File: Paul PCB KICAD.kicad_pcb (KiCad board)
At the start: 2 copper layers, 81 parts, among them U1 ATmega32U4-AU

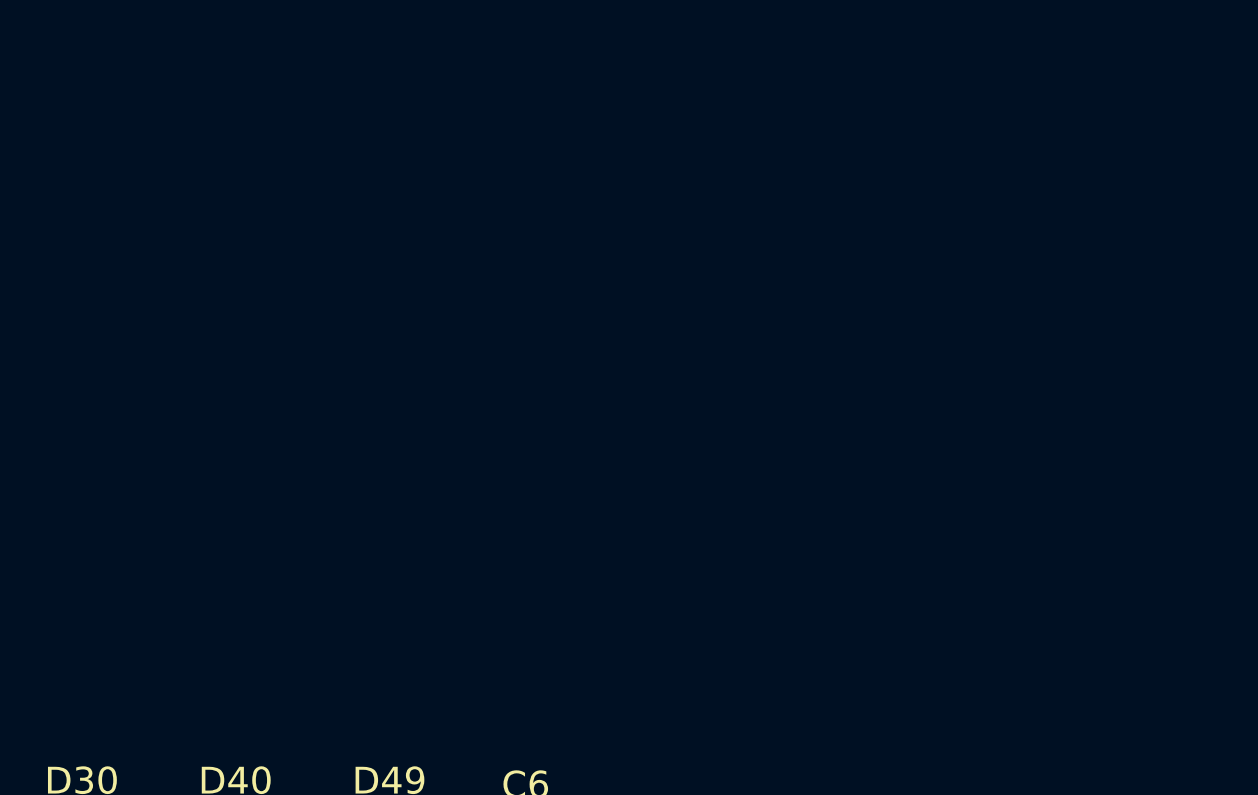
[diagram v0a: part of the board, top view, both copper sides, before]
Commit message: Updated USB to 4084 GCT
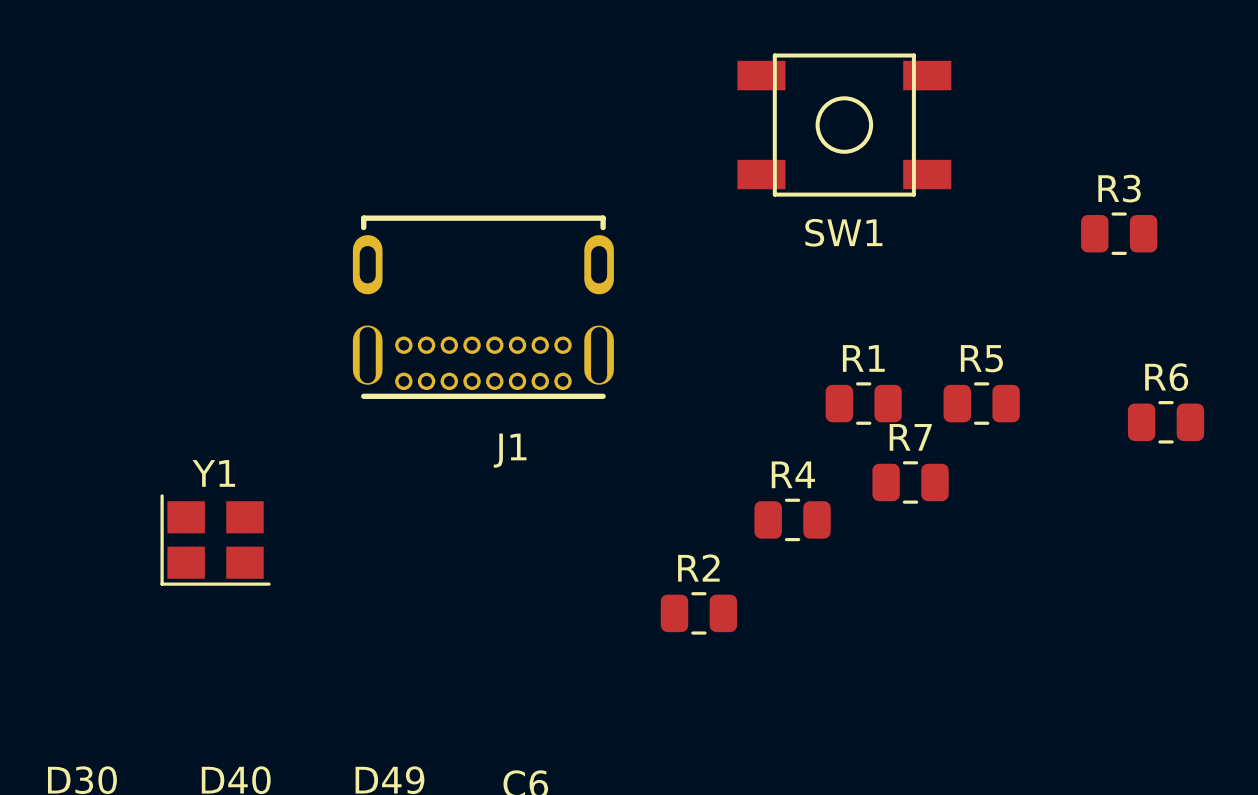
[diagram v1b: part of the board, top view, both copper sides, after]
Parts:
- added J1: USB4085-GF-A_REVA, 4085 USB Connector GCT:GCT_USB4085-GF-A_REVA, F.Cu at (105.6, 70.6)
- added R1: 1M, Resistor_SMD:R_0805_2012Metric, F.Cu at (119.8, 75.5)
- added R2: 5.1k, Resistor_SMD:R_0805_2012Metric, F.Cu at (113.6, 83.3)
- added R3: 5.1k, Resistor_SMD:R_0805_2012Metric, F.Cu at (129.3, 69.2)
- added R4: 22, Resistor_SMD:R_0805_2012Metric, F.Cu at (117.1, 79.8)
- added R5: 22, Resistor_SMD:R_0805_2012Metric, F.Cu at (124.2, 75.5)
- added R6: 10k, Resistor_SMD:R_0805_2012Metric, F.Cu at (131.1, 76.2)
- added R7: 10k, Resistor_SMD:R_0805_2012Metric, F.Cu at (121.5, 78.5)
- added SW1: SW_Push, random-keyboard-parts:SKQG-1155865, F.Cu at (119.1, 65.1)
- added Y1: 16MHz, Crystal:Crystal_SMD_3225-4Pin_3.2x2.5mm, F.Cu at (95.6, 80.6)
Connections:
- C1 pad 1: Net-(C1-Pad1) -> GND
- C1 pad 2: GND -> Net-(C1-Pad2)

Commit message: Added Near Final Edge Cut and Positioned Switch footprints
Need to add the diodes and caps and some cleanup
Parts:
- removed J1: USB4085-GF-A_REVA, 4085 USB Connector GCT:GCT_USB4085-GF-A_REVA
- added MX1: MX-NoLED, MX_Only:MXOnly-1U-Hotswap, F.Cu at (26.7, -83.2)
- added MX10: MX-NoLED, MX_Only:MXOnly-1U-Hotswap, F.Cu at (209.6, -82.6)
- added MX100: MX-NoLED, MX_Only:MXOnly-1.5U-Hotswap, F.Cu at (9.96, -64.1)
- added MX101: MX-NoLED, MX_Only:MXOnly-1U-Hotswap, F.Cu at (33.8, -64.1)
- added MX102: MX-NoLED, MX_Only:MXOnly-1U-Hotswap, F.Cu at (54.0, -64.0)
- added MX103: MX-NoLED, MX_Only:MXOnly-1U-Hotswap, F.Cu at (72.9, -61.3)
- added MX104: MX-NoLED, MX_Only:MXOnly-1U-Hotswap, F.Cu at (91.7, -58.7)
- added MX105: MX-NoLED, MX_Only:MXOnly-1U-Hotswap, F.Cu at (110.6, -56.0)
- added MX106: MX-NoLED, MX_Only:MXOnly-1U-Hotswap, F.Cu at (146.2, -54.4)
- added MX107: MX-NoLED, MX_Only:MXOnly-1U-Hotswap, F.Cu at (165.1, -57.1)
- added MX108: MX-NoLED, MX_Only:MXOnly-1U-Hotswap, F.Cu at (183.9, -59.7)
- added MX109: MX-NoLED, MX_Only:MXOnly-1U-Hotswap, F.Cu at (202.8, -62.4)
- added MX11: MX-NoLED, MX_Only:MXOnly-1U-Hotswap, F.Cu at (229.8, -83.2)
- added MX110: MX-NoLED, MX_Only:MXOnly-1U-Hotswap, F.Cu at (223.1, -64.1)
- added MX111: MX-NoLED, MX_Only:MXOnly-1U-Hotswap, F.Cu at (242.2, -64.1)
- added MX112: MX-NoLED, MX_Only:MXOnly-1U-Hotswap, F.Cu at (261.2, -64.1)
- added MX113: MX-NoLED, MX_Only:MXOnly-1.5U-Hotswap, F.Cu at (285.0, -64.1)
- added MX114: MX-NoLED, Rotary_Encoder:RotaryEncoder_Alps_EC11E-Switch_Vertical_H20mm, F.Cu at (308.6, -85.7)
- added MX12: MX-NoLED, MX_Only:MXOnly-1U-Hotswap, F.Cu at (248.8, -83.2)
- added MX13: MX-NoLED, MX_Only:MXOnly-1U-Hotswap, F.Cu at (267.9, -83.2)
- added MX14: MX-NoLED, MX_Only:MXOnly-1U-Hotswap, F.Cu at (286.9, -83.2)
- added MX2: MX-NoLED, MX_Only:MXOnly-1U-Hotswap, F.Cu at (47.2, -84.2)
- added MX200: MX-NoLED, MX_Only:MXOnly-1.75U-Hotswap, F.Cu at (9.66, -45.1)
- added MX201: MX-NoLED, MX_Only:MXOnly-1U-Hotswap, F.Cu at (35.9, -45.1)
- added MX202: MX-NoLED, MX_Only:MXOnly-1U-Hotswap, F.Cu at (56.1, -44.4)
- added MX203: MX-NoLED, MX_Only:MXOnly-1U-Hotswap, F.Cu at (74.9, -41.8)
- added MX204: MX-NoLED, MX_Only:MXOnly-1U-Hotswap, F.Cu at (93.8, -39.1)
- added MX205: MX-NoLED, MX_Only:MXOnly-1U-Hotswap, F.Cu at (112.7, -36.5)
- added MX206: MX-NoLED, MX_Only:MXOnly-1U-Hotswap, F.Cu at (153.6, -36.2)
- added MX207: MX-NoLED, MX_Only:MXOnly-1U-Hotswap, F.Cu at (172.5, -38.9)
- added MX208: MX-NoLED, MX_Only:MXOnly-1U-Hotswap, F.Cu at (191.3, -41.5)
- added MX209: MX-NoLED, MX_Only:MXOnly-1U-Hotswap, F.Cu at (210.2, -44.2)
- added MX210: MX-NoLED, MX_Only:MXOnly-1U-Hotswap, F.Cu at (230.3, -45.1)
- added MX211: MX-NoLED, MX_Only:MXOnly-1U-Hotswap, F.Cu at (249.3, -45.1)
- added MX212: MX-NoLED, MX_Only:MXOnly-2.25U-Hotswap, F.Cu at (280.3, -45.1)
- added MX214: MX-NoLED, MX_Only:MXOnly-1U-Hotswap, F.Cu at (316.1, -59.8)
- added MX3: MX-NoLED, MX_Only:MXOnly-1U-Hotswap, F.Cu at (66.1, -81.5)
- added MX300: MX-NoLED, MX_Only:MXOnly-2.25U-Hotswap, F.Cu at (11.7, -26.0)
- added MX301: MX-NoLED, MX_Only:MXOnly-1U-Hotswap, F.Cu at (42.7, -26.0)
- added MX302: MX-NoLED, MX_Only:MXOnly-1U-Hotswap, F.Cu at (62.8, -24.3)
- added MX303: MX-NoLED, MX_Only:MXOnly-1U-Hotswap, F.Cu at (81.7, -21.6)
- added MX304: MX-NoLED, MX_Only:MXOnly-1U-Hotswap, F.Cu at (100.6, -19.0)
- added MX305: MX-NoLED, MX_Only:MXOnly-1U-Hotswap, F.Cu at (119.4, -16.3)
- added MX306: MX-NoLED, MX_Only:MXOnly-1U-Hotswap, F.Cu at (165.7, -18.7)
- added MX307: MX-NoLED, MX_Only:MXOnly-1U-Hotswap, F.Cu at (184.5, -21.4)
- added MX308: MX-NoLED, MX_Only:MXOnly-1U-Hotswap, F.Cu at (203.4, -24.0)
- added MX309: MX-NoLED, MX_Only:MXOnly-1U-Hotswap, F.Cu at (223.1, -26.0)
- added MX310: MX-NoLED, MX_Only:MXOnly-1U-Hotswap, F.Cu at (242.2, -26.0)
- added MX311: MX-NoLED, MX_Only:MXOnly-1U-Hotswap, F.Cu at (261.2, -26.0)
- added MX312: MX-NoLED, MX_Only:MXOnly-1U-Hotswap, F.Cu at (285.2, -21.1)
- added MX314: MX-NoLED, MX_Only:MXOnly-1U-Hotswap, F.Cu at (316.1, -40.7)
- added MX4: MX-NoLED, MX_Only:MXOnly-1U-Hotswap, F.Cu at (85.0, -78.9)
- added MX400: MX-NoLED, MX_Only:MXOnly-1.25U-Hotswap, F.Cu at (6.98, -6.98)
- added MX401: MX-NoLED, MX_Only:MXOnly-1.25U-Hotswap, F.Cu at (30.8, -7.00)
- added MX402: MX-NoLED, MX_Only:MXOnly-1.25U-Hotswap, F.Cu at (62.6, -5.06)
- added MX404: MX-NoLED, MX_Only:MXOnly-2.75U-Hotswap-ReversedStabilizers, F.Cu at (100.3, 0.24)
- added MX405: MX-NoLED, MX_Only:MXOnly-1U-Hotswap, F.Cu at (146.8, -16.1)
- added MX406: MX-NoLED, MX_Only:MXOnly-2.25U-Hotswap-ReversedStabilizers, F.Cu at (170.7, -0.17)
- added MX408: MX-NoLED, MX_Only:MXOnly-1U-Hotswap, F.Cu at (201.3, -4.48)
- added MX409: MX-NoLED, MX_Only:MXOnly-1U-Hotswap, F.Cu at (223.1, -7.01)
- added MX410: MX-NoLED, MX_Only:MXOnly-1U-Hotswap, F.Cu at (242.2, -7.01)
- added MX411: MX-NoLED, MX_Only:MXOnly-1U-Hotswap, F.Cu at (266.2, -2.06)
- added MX412: MX-NoLED, MX_Only:MXOnly-1U-Hotswap, F.Cu at (285.2, -2.05)
- added MX414: MX-NoLED, MX_Only:MXOnly-1U-Hotswap, F.Cu at (304.2, -2.06)
- added MX5: MX-NoLED, MX_Only:MXOnly-1U-Hotswap, F.Cu at (103.8, -76.2)
- added MX6: MX-NoLED, MX_Only:MXOnly-1U-Hotswap, F.Cu at (122.7, -73.6)
- added MX7: MX-NoLED, MX_Only:MXOnly-1U-Hotswap, F.Cu at (153.0, -74.6)
- added MX8: MX-NoLED, MX_Only:MXOnly-1U-Hotswap, F.Cu at (171.9, -77.3)
- added MX9: MX-NoLED, MX_Only:MXOnly-1U-Hotswap, F.Cu at (190.7, -79.9)
- added USB1: HRO-TYPE-C-31-M-12, Type-C:HRO-TYPE-C-31-M-12, F.Cu at (159.5, -101.3)
- moved MX0 186.8 mm to (7.67, -83.2)
- moved D4 164.9 mm to (81.1, -73.2)
- moved U1 149.5 mm to (129.7, -48.5), turned to 270 degrees
- moved R3 41.8 mm to (87.7, 72.8)
- moved R1 36.6 mm to (83.3, 72.8)
- moved C1 34.2 mm to (83.3, 69.8)
- moved R2 29.2 mm to (87.8, 69.8)
- renumbered D1 to D0, D6 to D1, D49 to D10, D2 to D100, D7 to D101, D12 to D102, D17 to D103, D21 to D104, D26 to D105, D31 to D106, D36 to D107, D40 to D108, D45 to D109, D54 to D11, D50 to D110, D55 to D111, D60 to D112, D65 to D113, D67 to D114, D59 to D12, D64 to D13, D66 to D14, D11 to D2, D3 to D200, D8 to D201, D13 to D202, D18 to D203, D22 to D204, D27 to D205, D32 to D206, D37 to D207, D41 to D208, D46 to D209, D51 to D210, D56 to D211, D61 to D212, D68 to D214, D16 to D3, D4 to D300, D9 to D301, D14 to D302, D19 to D303, D23 to D304, D28 to D305, D33 to D306, D38 to D307, D42 to D308, D47 to D309, D52 to D310, D57 to D311, D62 to D312, D69 to D314, D20 to D4, D5 to D400, D10 to D401, D15 to D402, D24 to D404, D29 to D405, D34 to D406, D43 to D408, D48 to D409, D53 to D410, D58 to D411, D63 to D412, D70 to D414, D25 to D5, D30 to D6, D35 to D7, D39 to D8, D44 to D9, MX1 to MX0
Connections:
- U1 pad 15: GND -> Net-(U1-Pad15)
- U1 pad 23: GND -> Net-(U1-Pad15)
- U1 pad 35: GND -> Net-(U1-Pad15)
- U1 pad 43: GND -> Net-(U1-Pad15)
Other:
- board outline added: 330.9 x 112.7 mm

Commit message: More PCB Completed
Added Mounting Holes as pads
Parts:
- removed MX114: MX-NoLED, Rotary_Encoder:RotaryEncoder_Alps_EC11E-Switch_Vertical_H20mm
- added 2.5: 2.5_Mount, MountingHole:MountingHole_2.5mm_Pad, F.Cu at (133.1, -35.4)
- added 2.5: 2.5_Mount, MountingHole:MountingHole_2.5mm_Pad, F.Cu at (17.2, -80.2)
- added 2.5: 2.5_Mount, MountingHole:MountingHole_2.5mm_Pad, F.Cu at (232.6, -16.5)
- added 2.5: 2.5_Mount, MountingHole:MountingHole_2.5mm_Pad, F.Cu at (301.5, -83.2)
- added 2.5: 2.5_Mount, MountingHole:MountingHole_2.5mm_Pad, F.Cu at (1.15, -54.6)
- added 2.5: 2.5_Mount, MountingHole:MountingHole_2.5mm_Pad, F.Cu at (77.3, -3.00)
- added 2.5: 2.5_Mount, MountingHole:MountingHole_2.5mm_Pad, F.Cu at (219.9, -80.4)
- added 2.5: 2.5_Mount, MountingHole:MountingHole_2.5mm_Pad, F.Cu at (18.9, -7.00)
- added 2.5: 2.5_Mount, MountingHole:MountingHole_2.5mm_Pad, F.Cu at (162.9, -73.0)
- added 2.5: 2.5_Mount, MountingHole:MountingHole_2.5mm_Pad, F.Cu at (294.8, -11.6)
- added 2.5: 2.5_Mount, MountingHole:MountingHole_2.5mm_Pad, F.Cu at (94.0, -74.6)
- added 2.5: 2.5_Mount, MountingHole:MountingHole_2.5mm_Pad, F.Cu at (149.4, 2.33)
- added 2.5: 2.5_Mount, MountingHole:MountingHole_2.5mm_Pad, F.Cu at (302.3, -47.4)
- added RotaryEncoder1: Rotary_Encoder_Switch, Rotary_Encoder:RotaryEncoder_Alps_EC11E-Switch_Vertical_H20mm, F.Cu at (323.6, -80.7)
- C1, C2, C3, C4, C5, C6, C7, C8, D0, D1, D10, D100, D101, D102, D103, D104, D105, D106, D107, D108, D109, D11, D110, D111, D112, D113, D114, D12, D13, D14, D2, D200, D201, D202, D203, D204, D205, D206, D207, D208, D209, D210, D211, D212, D214, D3, D300, D301, D302, D303, D304, D305, D306, D307, D308, D309, D310, D311, D312, D314, D4, D400, D401, D402, D404, D405, D406, D408, D409, D410, D411, D412, D414, D5, D6, D7, D8, D9, R1, R6, R7, U1, Y1: moved to B.Cu
- moved D114 291.8 mm to (307.2, -73.8)
- moved D214 275.0 mm to (316.7, -54.8)
- moved D13 272.1 mm to (266.7, -78.6)
- moved D314 260.2 mm to (316.7, -33.3)
- moved D12 259.9 mm to (252.4, -78.6), turned to 270 degrees
- moved D14 256.7 mm to (288.1, -78.6)
- moved D111 251.8 mm to (242.9, -57.1)
- moved D113 248.7 mm to (285.8, -59.5)
- moved D11 247.9 mm to (231.0, -76.2)
- moved D414 242.7 mm to (307.2, 2.38)
- moved D212 239.7 mm to (281.0, -40.5)
- moved D312 229.0 mm to (288.1, -16.7)
- moved D412 226.3 mm to (290.5, 2.38), turned to 270 degrees
- moved D310 224.3 mm to (242.9, -21.4)
- moved D410 222.5 mm to (242.9, -2.38)
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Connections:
- net Net-(R4-Pad1) renamed /USB_N
- net Net-(R5-Pad1) renamed /USB_P
- D114 pad 2: Net-(D114-Pad2) -> Rot.Enc.2
- U1 pad 15: Net-(U1-Pad15) -> GND
- U1 pad 23: Net-(U1-Pad15) -> GND
- U1 pad 35: Net-(U1-Pad15) -> GND
- U1 pad 43: Net-(U1-Pad15) -> GND
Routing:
- net +5V: track 0.00 -> 123.3 mm, vias 0 -> 4
- net COL5: track 0.00 -> 97.8 mm, vias 0 -> 5
- net COL1: track 0.00 -> 87.8 mm, vias 0 -> 5
- net COL4: track 0.00 -> 85.6 mm, vias 0 -> 5
- net COL2: track 0.00 -> 85.6 mm, vias 0 -> 5
- net COL0: track 0.00 -> 82.1 mm, vias 0 -> 5
- net COL3: track 0.00 -> 66.3 mm, vias 0 -> 4
- net /USB_N: track 0.00 -> 54.5 mm, vias 0 -> 1
- net GND: track 0.00 -> 53.3 mm, vias 0 -> 5
- net /USB_P: track 0.00 -> 52.5 mm, vias 0 -> 3
- net Net-(C1-Pad2): track 0.00 -> 28.5 mm
- net VCC: track 0.00 -> 19.2 mm, vias 0 -> 2
- net Net-(C3-Pad1): track 0.00 -> 15.6 mm
- net Net-(C4-Pad1): track 0.00 -> 12.8 mm
- net D+: track 0.00 -> 9.04 mm
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- added copper zone on F.Cu, net GND
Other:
- outline, holes or cut-outs redrawn
- net class Power added: clearance 0.2, trace_width 0.4, via_dia 0.8, via_drill 0.4
- board text added: "MX114"

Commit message: Further Completion
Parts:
- R2, R3, SW1: moved to B.Cu
- moved SW1 42.5 mm to (140.1, -68.2), turned to 90 degrees
- moved R6 36.9 mm to (136.1, -65.6), turned to 90 degrees
- moved R4 23.8 mm to (138.8, -78.6), turned to 23.5 degrees
- moved R5 21.9 mm to (139.6, -76.7), turned to 23.5 degrees
- moved R1 14.9 mm to (166.1, -85.8), turned to 156.5 degrees
- moved D107 14.6 mm to (173.2, -63.0), turned to 278 degrees
- moved C1 14.4 mm to (166.9, -87.6), turned to 156.5 degrees
- moved D111 14.3 mm to (251.1, -68.8), turned to 270 degrees
- moved D102 13.5 mm to (63.3, -67.5), turned to 262 degrees
- moved D101 13.1 mm to (42.6, -68.8), turned to 270 degrees
- moved D103 13.1 mm to (82.2, -64.8), turned to 262 degrees
- moved D109 12.8 mm to (210.9, -68.3), turned to 278 degrees
- moved D104 12.7 mm to (101.0, -62.1), turned to 262 degrees
- moved D108 12.6 mm to (192.0, -65.7), turned to 278 degrees
- moved D112 12.6 mm to (270.4, -68.8), turned to 270 degrees
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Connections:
- net /USB_N renamed /Data_N
- net /USB_P renamed /Data_P
- net Net-(R6-Pad2) renamed /Reset
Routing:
- net ROW0: track 0.00 -> 288.1 mm
- net COL14: track 0.00 -> 128.9 mm
- net ROW1: track 0.00 -> 113.7 mm
- net COL6: track 0.00 -> 108.9 mm, vias 5 -> 7
- net COL12: track 0.00 -> 100.0 mm
- net GND: track 53.3 -> 153.1 mm, vias 5 -> 7
- net COL11: track 0.00 -> 96.2 mm
- net COL10: track 0.00 -> 89.6 mm
- net COL8: track 0.00 -> 86.7 mm
- net COL9: track 0.00 -> 85.5 mm
- net COL7: track 0.00 -> 66.3 mm
- net /Reset: track 0.00 -> 29.0 mm, vias 0 -> 2
- net COL13: track 0.00 -> 28.8 mm
- net /Data_N: track 54.5 -> 29.5 mm
- net /Data_P: track 52.5 -> 29.5 mm, vias 3 -> 1
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- added copper zone on B.Cu, net GND
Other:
- board size 330.9 x 112.7 mm -> 330.9 x 105.7 mm
- board text added: "Designed by Alfie Lockrey June 2021"
- board text added: "PaulPCB - V1.0"

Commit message: Finished Prelim Diode Placement
Beginning to Route Tracks
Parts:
- removed MX3: MX-NoLED, MX_Only:MXOnly-1U-Hotswap
- moved D214 24.0 mm to (292.7, -55.5)
- moved D314 18.3 mm to (298.4, -32.6)
- moved D206 15.1 mm to (161.4, -42.1), turned to 278 degrees
- moved D400 14.8 mm to (15.6, -12.8), turned to 90 degrees
- moved D307 14.6 mm to (192.5, -27.2), turned to 278 degrees
- moved D306 14.4 mm to (173.6, -24.6), turned to 278 degrees
- moved D304 14.4 mm to (109.9, -22.4), turned to 262 degrees
- moved D408 14.4 mm to (209.2, -10.3), turned to 278 degrees
- moved D311 14.3 mm to (270.1, -30.8), turned to 270 degrees
- moved D405 14.3 mm to (154.7, -21.9), turned to 98 degrees
- moved D210 14.2 mm to (238.9, -49.8), turned to 270 degrees
- moved D305 14.1 mm to (128.7, -19.8), turned to 262 degrees
- moved D411 14.1 mm to (274.9, -6.74), turned to 270 degrees
- moved D203 14.1 mm to (84.2, -45.3), turned to 262 degrees
- moved D204 13.8 mm to (103.1, -42.5), turned to 262 degrees
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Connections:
- D408 pad 1: Net-(D408-Pad1) -> ROW4
- MX408 pad 2: Net-(MX408-Pad2) -> Net-(D408-Pad2)
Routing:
- net ROW1: track 113.7 -> 281.4 mm
- net ROW2: track 0.00 -> 114.1 mm
- net Net-(D201-Pad2): track 0.00 -> 4.08 mm
- net Net-(D200-Pad2): track 0.00 -> 4.02 mm

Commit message: Finished V1.0
I think it may be done
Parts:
- added MX3: MX-NoLED, MX_Only:MXOnly-1U-Hotswap, F.Cu at (66.1, -81.5)
- F1, R4, R5: moved to B.Cu
- moved C6 4.09 mm to (137.6, -41.8), turned to 90 degrees
- moved C3 3.12 mm to (149.2, -46.8)
- moved C4 3.12 mm to (149.2, -49.6)
- moved Y1 3.12 mm to (144.6, -48.2)
- moved C8 1.22 mm to (125.4, -59.4)
- moved D414 1.16 mm to (295.4, 1.01)
- moved SW1 1.09 mm to (140.1, -69.2)
- moved R3 0.74 mm to (162.4, -82.4), turned to 180 degrees
- moved D409 0.74 mm to (226.4, -15.9)
- moved D400 0.74 mm to (15.5, -12.1), turned to 270 degrees
- moved C1 0.41 mm to (167.3, -87.5)
- moved R1 0.41 mm to (166.5, -85.7)
- moved C5 0.34 mm to (139.4, -51.2)
- moved R2 0.33 mm to (162.4, -84.4), turned to 180 degrees
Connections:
- RotaryEncoder1 pad C: Rot.Enc.C -> GND
- U1 pad 10: Net-(U1-Pad10) -> COL6
- U1 pad 11: Net-(U1-Pad11) -> COL7
- U1 pad 12: Net-(U1-Pad12) -> COL13
- U1 pad 18: Net-(U1-Pad18) -> COL8
- U1 pad 19: Net-(U1-Pad19) -> COL9
- U1 pad 20: Net-(U1-Pad20) -> COL10
- U1 pad 21: Net-(U1-Pad21) -> COL11
- U1 pad 22: Net-(U1-Pad22) -> ROW2
- U1 pad 25: Net-(U1-Pad25) -> Rot.Enc.A
- U1 pad 26: Net-(U1-Pad26) -> Rot.Enc.B
- U1 pad 27: Net-(U1-Pad27) -> COL12
- U1 pad 28: Net-(U1-Pad28) -> COL14
- U1 pad 29: Net-(U1-Pad29) -> ROW3
- U1 pad 30: Net-(U1-Pad30) -> ROW4
- U1 pad 36: Net-(U1-Pad36) -> COL0
- U1 pad 37: Net-(U1-Pad37) -> COL1
- U1 pad 38: Net-(U1-Pad38) -> COL2
- U1 pad 39: Net-(U1-Pad39) -> COL3
- U1 pad 40: Net-(U1-Pad40) -> COL4
- U1 pad 41: Net-(U1-Pad41) -> COL5
- U1 pad 8: Net-(U1-Pad8) -> ROW1
- U1 pad 9: Net-(U1-Pad9) -> ROW0
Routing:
- net ROW4: track 0.00 -> 498.3 mm
- net ROW3: track 0.00 -> 339.6 mm
- net GND: track 153.1 -> 400.8 mm
- net Rot.Enc.A: track 0.00 -> 241.1 mm
- net Rot.Enc.B: track 0.00 -> 237.3 mm
- net ROW2: track 114.1 -> 328.2 mm, vias 0 -> 2
- net COL14: track 128.9 -> 322.5 mm, vias 4 -> 5
- net COL12: track 100.0 -> 265.5 mm, vias 5 -> 6
- net COL13: track 28.8 -> 182.4 mm, vias 2 -> 5
- net COL0: track 82.1 -> 204.1 mm, vias 5 -> 6
- net COL11: track 96.2 -> 207.8 mm, vias 5 -> 6
- net COL1: track 87.8 -> 188.0 mm, vias 5 -> 6
- net COL10: track 89.6 -> 182.0 mm, vias 5 -> 6
- net COL2: track 85.6 -> 163.3 mm, vias 5 -> 6
- net COL9: track 85.5 -> 155.9 mm, vias 5 -> 6
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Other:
- board text added: "A"
- board text added: "B"
- board text added: "C"
- board text added: "What are you looking at?"

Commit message: Added Ground Fill and Changed Reset Switch
Added Ground Fill and Changed Reset Switch
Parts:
- SW1: footprint random-keyboard-parts:SKQG-1155865 -> TS-1187A-B-A-B:SW_TS-1187A-B-A-B
- moved SW1 0.98 mm to (140.7, -70.0), turned to 270 degrees
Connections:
- 2.5 pad 1: (no net) -> Net-(C1-Pad2)
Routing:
- net Net-(C1-Pad2): track 21.7 -> 38.0 mm, vias 0 -> 1
- net /Reset: track 30.7 -> 40.0 mm
- net GND: track 400.8 -> 407.4 mm, vias 7 -> 12
